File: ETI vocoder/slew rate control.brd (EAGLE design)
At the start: 57.1 x 33.6 mm, 28 parts, among them CN1 NMJ6HCD2, IC1 LM556N, Q1 2N3904, Q2 2N3906, X1 22-23-2031

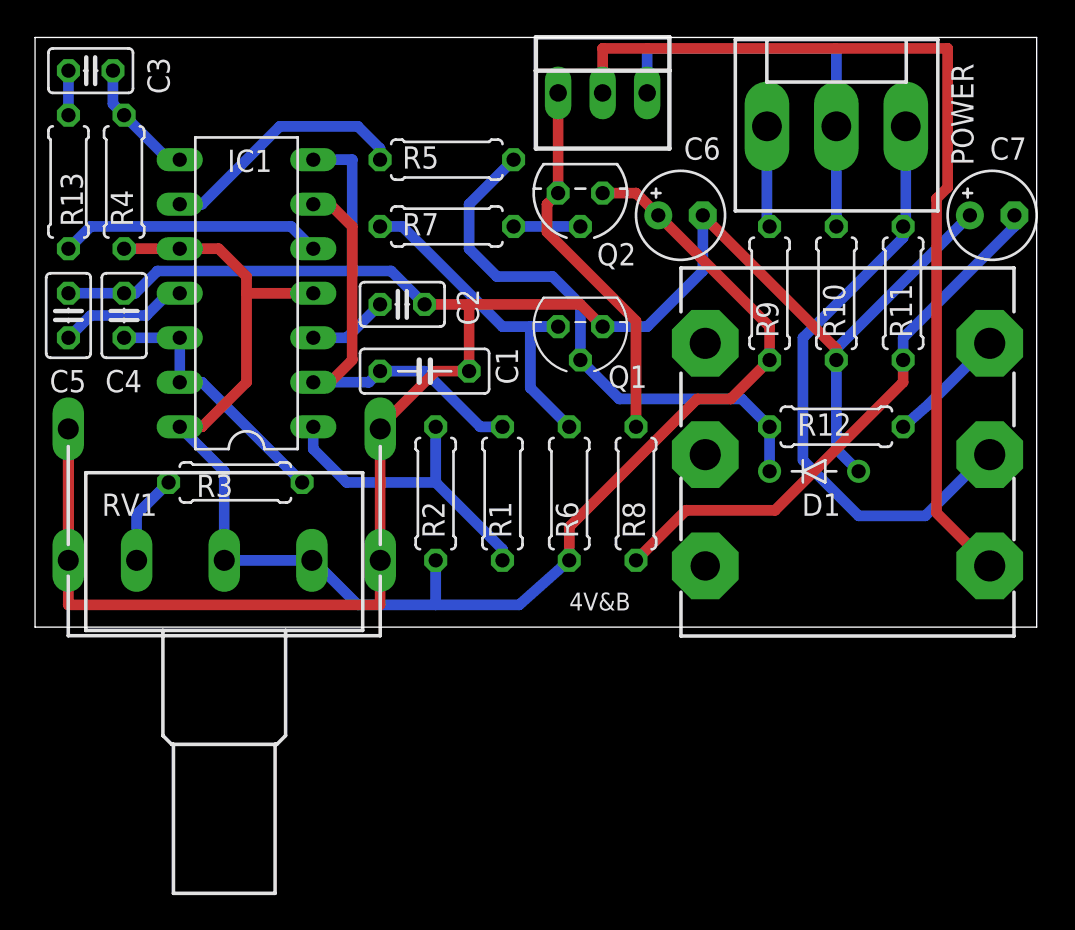
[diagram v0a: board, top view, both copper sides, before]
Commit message: All ETI boards checked for caps and pots
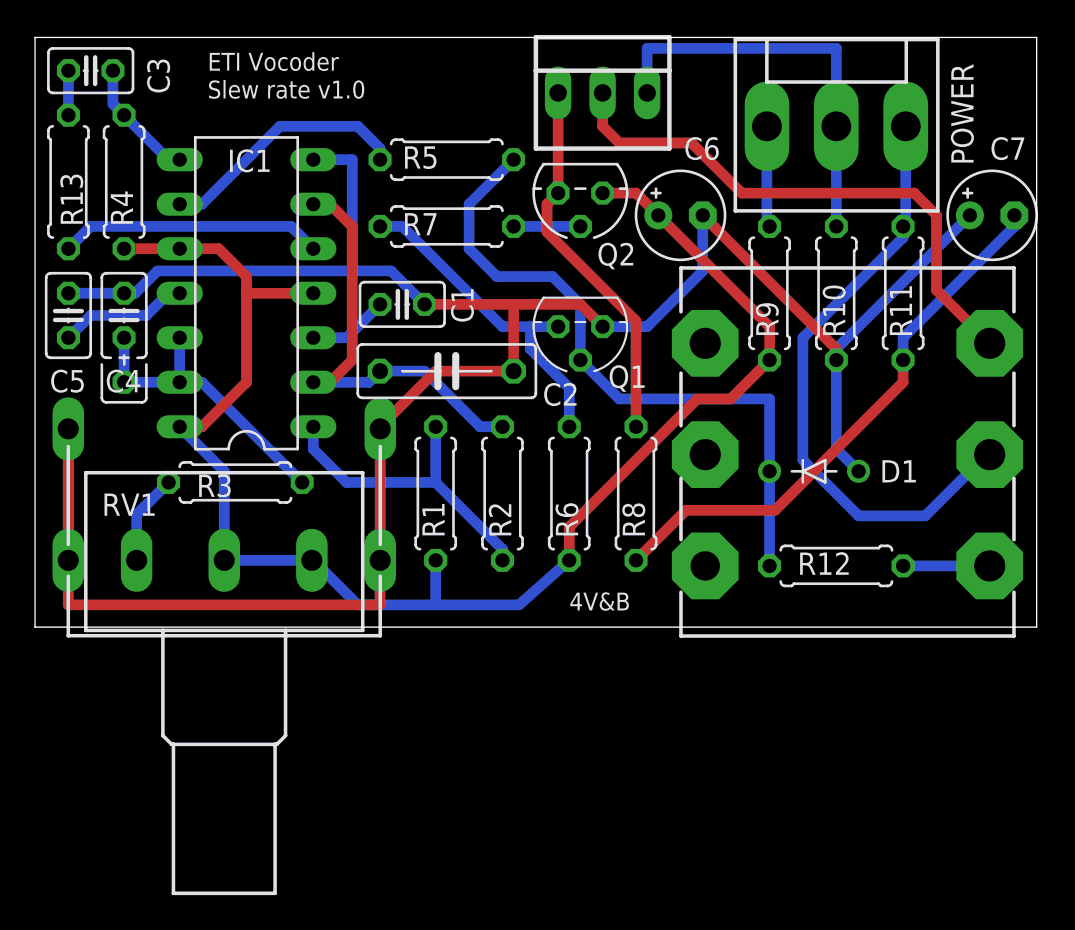
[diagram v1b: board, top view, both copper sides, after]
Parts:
- C2: device resistor:C050-025X075 -> resistor:C075-032X103
- C4: device resistor:C025-025X050 -> resistor:C025_050-025X075
- moved R12 7.94 mm to (45.7, 3.49)
- moved C2 1.27 mm to (23.5, 14.6)
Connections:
- net FROM_V/UV_SWITCH: now also CN1.T; no longer CN1.S
- net N$13: now also CN1.S; no longer CN1.T
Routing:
- net FROM_V/UV_SWITCH: track 53.3 -> 31.6 mm
- net N$12: track 31.9 -> 38.2 mm
- net N$5: track 15.1 -> 17.6 mm
- net 0V: track 136.5 -> 139.0 mm
- net N$13: track 6.86 -> 4.94 mm
- net N$14: track 20.8 -> 19.2 mm
- net -12V: track 35.4 -> 34.9 mm
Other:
- board text added: "+12V"
- board text added: "-12V"
- board text added: "ETI Vocoder"
- board text added: "GND"
- board text added: "Out"
- board text added: "SW"
- board text added: "Slew rate v1.0"
